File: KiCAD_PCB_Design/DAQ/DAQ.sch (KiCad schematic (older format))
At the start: 92 parts

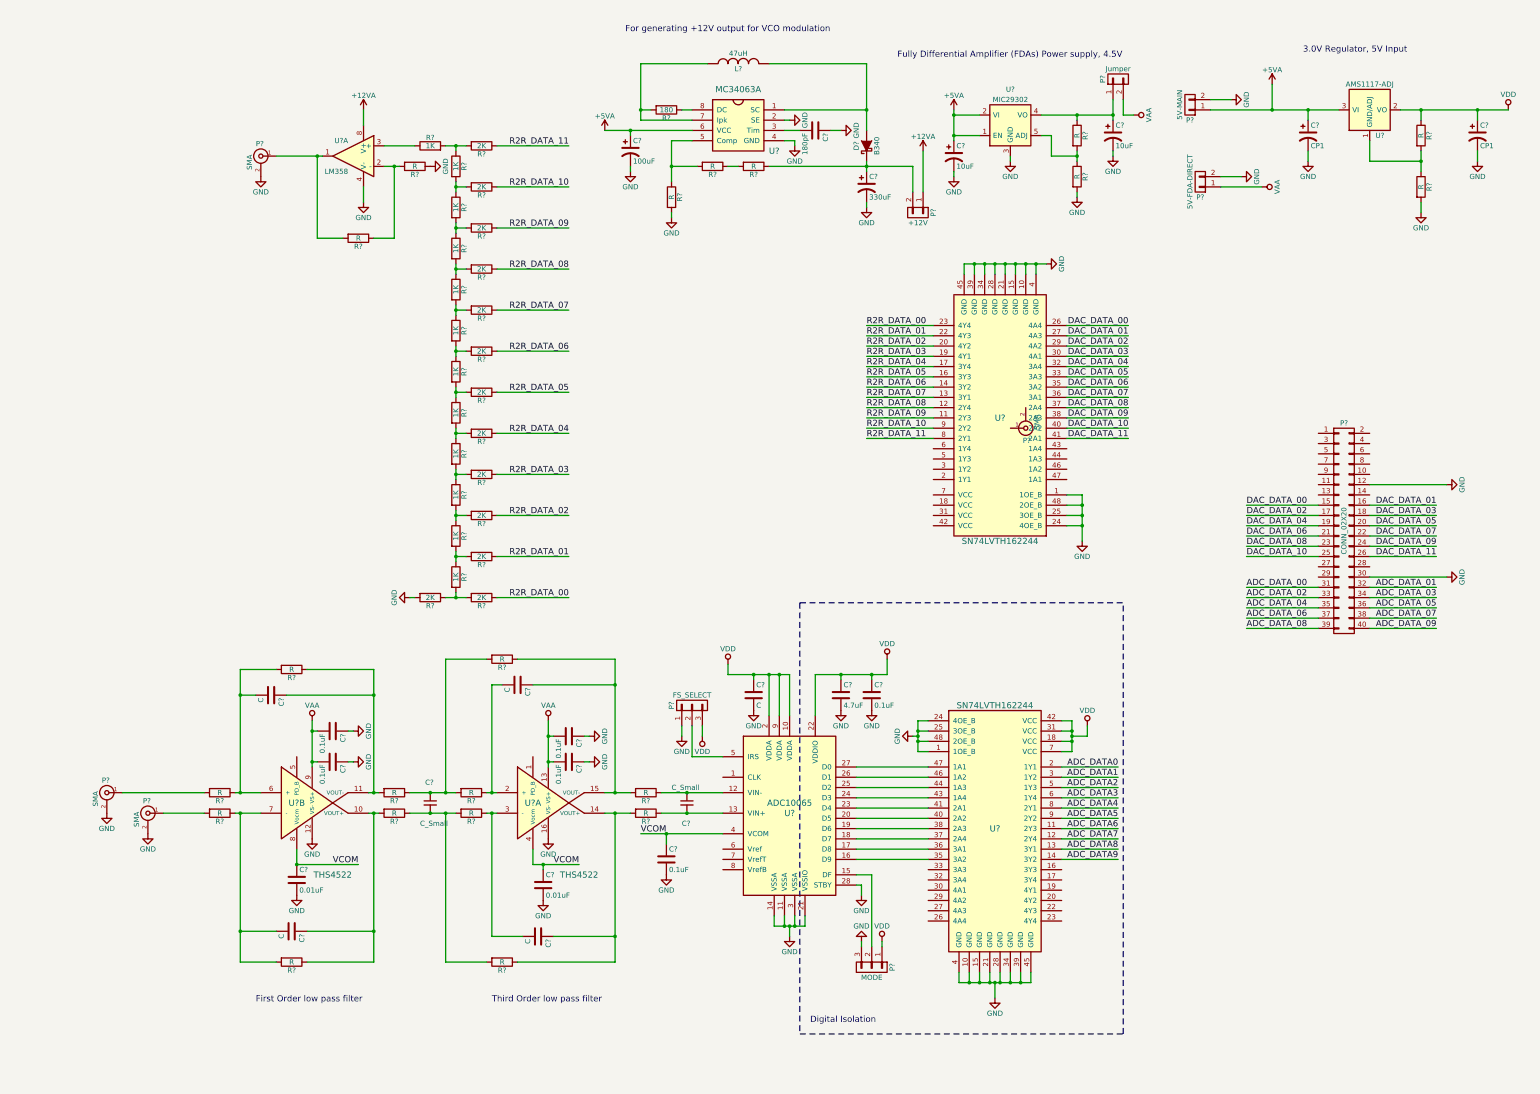
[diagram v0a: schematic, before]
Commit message: Schematic of DAQ.sch is almost complete, Making footprints of SMA, learning about patch array antennas
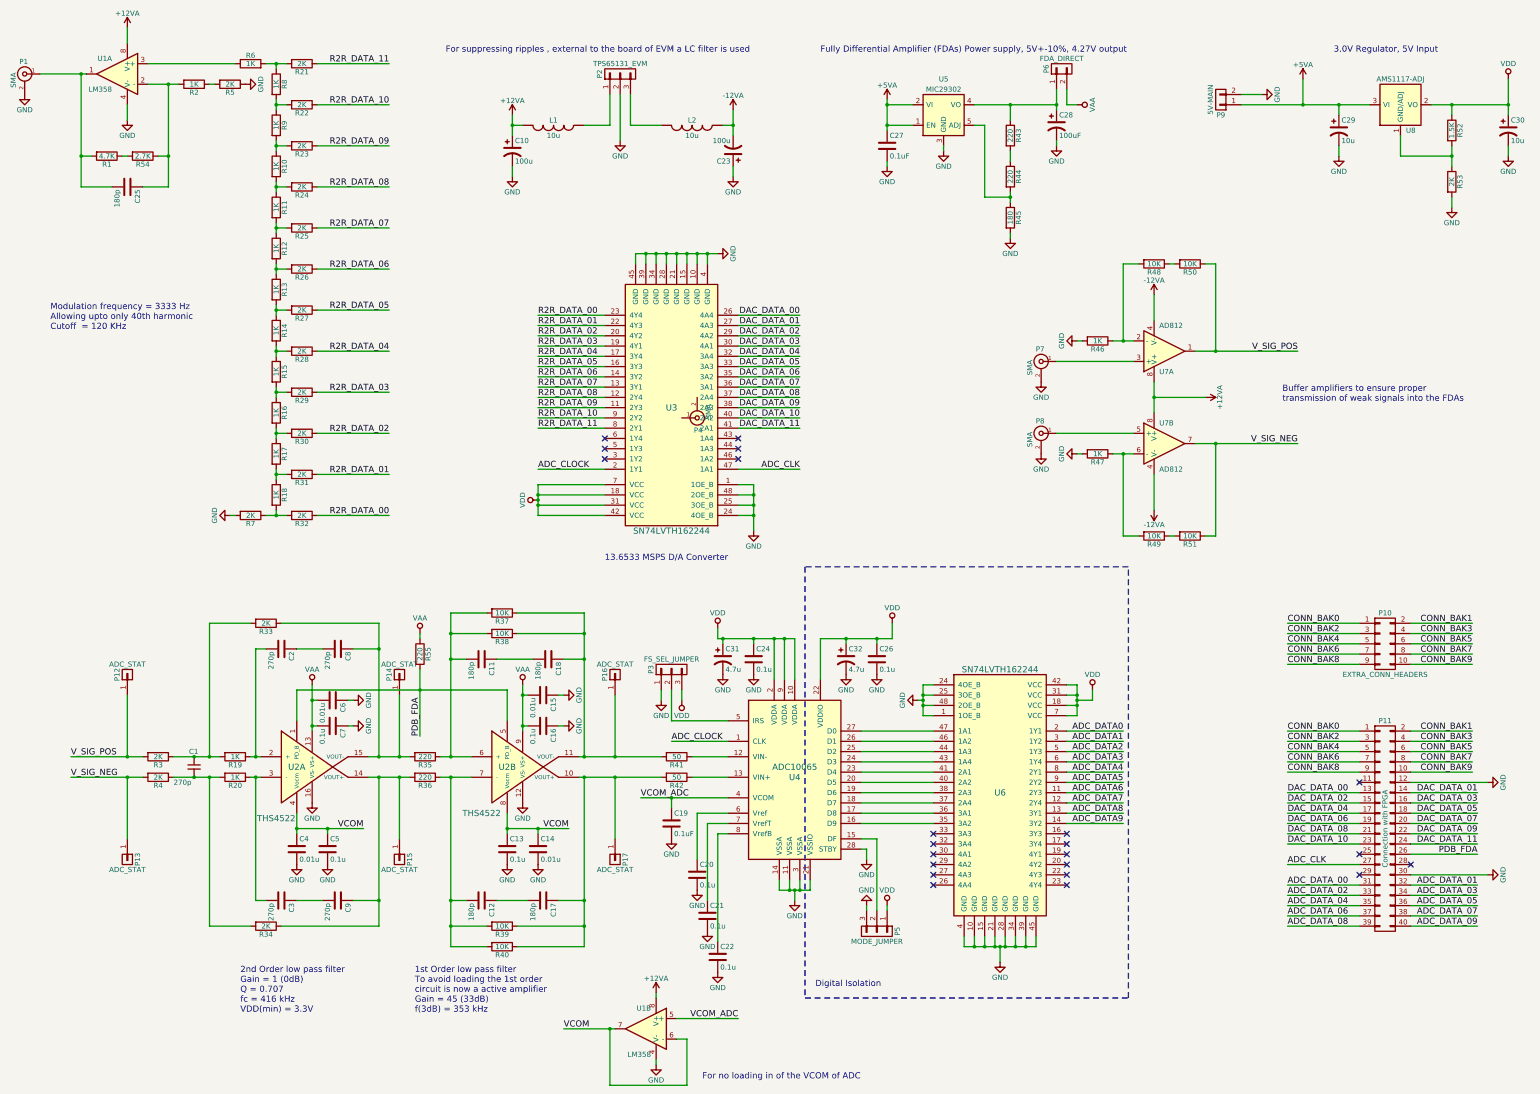
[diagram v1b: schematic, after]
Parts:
- removed C?: 4.7uF, symbol C
- removed C? (x2): C_Small, symbol C_Small
- removed C?: 0.01uF, symbol C
- removed C? (x3): C, symbol C
- removed C?: 10uF, symbol CP1
- removed C?: 100uF, symbol CP1
- removed C?: 330uF, symbol CP1
- removed C?: 180pF, symbol C
- removed D?: B340, symbol D_Schottky
- removed L?: 47uH, symbol INDUCTOR
- removed P?: +12V, symbol CONN_01X02
- removed P?: 5V-FDA-DIRECT, symbol CONN_01X02
- removed R? (x5): R, symbol R
- removed R?: 180, symbol R
- removed U? (x2): THS4522, symbol THS4522
- removed U?: MC34063A, symbol MC34063A
- added C1: 270p, symbol C_Small
- added C10, C23: 100u, symbol CP1
- added C11, C12, C17, C18, C25: 180p, symbol C
- added C13, C20, C21, C22, C5: 0.1u, symbol C
- added C14: 0.01u, symbol C
- added C27: 0.1uF, symbol C
- added C3, C8, C9: 270p, symbol C
- added C31, C32: 4.7u, symbol CP1
- added L1, L2: 10u, symbol INDUCTOR
- added P10: EXTRA_CONN_HEADERS, symbol CONN_02X05
- added P12, P13, P14, P15, P16, P17: ADC_STAT, symbol CONN_01X01
- added P2: TPS65131_EVM, symbol CONN_01X03
- added R2, R46, R47: 1K, symbol R
- added R37, R40, R48, R49, R50, R51: 10K, symbol R
- added R41, R42: 50, symbol R
- added R43, R55: 220, symbol R
- added R54: 2.7K, symbol R
- added unit 2 of U1
- added U2: THS4522, symbol THS4522
- added U7: AD812, symbol LM358
- C15, C6: renamed from C?; value 0.1uF -> 0.01u
- C16, C26, C7: renamed from C?; value 0.1uF -> 0.1u
- C2: renamed from C?; value C -> 270p
- C24: renamed from C?; value C -> 0.1u
- C28: renamed from C?; value 10uF -> 100uF; footprint (none) -> Capacitors_SMD:c_elec_6.3x5.3
- C29, C30: renamed from C?; value CP1 -> 10u
- C4: renamed from C?; value 0.01uF -> 0.01u
- P11: renamed from P?; value CONN_02X20 -> Connection with FPGA
- P3: renamed from P?; value FS_SELECT -> FS_SEL_JUMPER
- P5: renamed from P?; value MODE -> MODE_JUMPER
- P6: renamed from P?; value Jumper -> FDA_DIRECT
- R1: renamed from R?; value R -> 4.7K
- R19, R20: renamed from R?; value R -> 1K
- R3, R33, R34, R4, R5, R53: renamed from R?; value R -> 2K
- R35, R36, R44: renamed from R?; value R -> 220
- R38, R39: renamed from R?; value R -> 10K
- R45: renamed from R?; value R -> 180
- R52: renamed from R?; value R -> 1.5K
- gave numbers to parts that had none: 37
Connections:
- net +12VA: now also C10.1, L1.2, U1.8 (V+), U7.8 (V+), U7.8 (V+)
- net +5VA: now also C27.1
- net DAC_DATA_00: now also P11.13 (P13); no longer P11.15 (P15)
- net DAC_DATA_01: now also P11.14 (P14); no longer P11.16 (P16)
- net DAC_DATA_02: now also P11.15 (P15); no longer P11.17 (P17)
- net DAC_DATA_03: now also P11.16 (P16); no longer P11.18 (P18)
- net DAC_DATA_04: now also P11.17 (P17); no longer P11.19 (P19)
- net DAC_DATA_05: now also P11.18 (P18); no longer P11.20 (P20)
- net DAC_DATA_06: now also P11.19 (P19); no longer P11.21 (P21)
- net DAC_DATA_07: now also P11.20 (P20); no longer P11.22 (P22)
- net DAC_DATA_08: now also P11.21 (P21); no longer P11.23 (P23)
- net DAC_DATA_09: now also P11.22 (P22); no longer P11.24 (P24)
- net DAC_DATA_10: now also P11.23 (P23); no longer P11.25 (P25)
- net DAC_DATA_11: now also P11.24 (P24); no longer P11.26 (P26)
- net GND: now also C10.2, C13.2, C14.2, C20.2, C21.2, C22.2, C23.1, C27.2, C31.2, C32.2, C5.2, P2.2 (P2), R46.2, R47.2, U1.4 (V-), U2.12 (VS-), U2.16 (VS-)
- net VAA: now also R55.1, U2.13 (VS+), U2.9 (VS+)
- net VCOM: now also C13.1, C14.1, C5.1, U1.6 (-), U1.7, U2.4 (Vocm), U2.8 (Vocm); no longer C19.1, U4.4 (VCOM)
- net VDD: now also U3.18 (VCC), U3.31 (VCC), U3.42 (VCC), U3.7 (VCC), C31.1, C32.1
- net CONN_BAK0: now reaches P11.1 (P1)
- net CONN_BAK0: now also P10.1 (P1)
- net CONN_BAK9: now reaches P11.10 (P10)
- net CONN_BAK9: now also P10.10 (P10)
- net CONN_BAK1: now reaches P11.2 (P2)
- net CONN_BAK1: now also P10.2 (P2)
- net ADC_CLK: now reaches P11.27 (P27)
- net ADC_CLK: now also U3.47 (1A1)
- net CONN_BAK2: now reaches P11.3 (P3)
- net CONN_BAK2: now also P10.3 (P3)
- net CONN_BAK3: now reaches P11.4 (P4)
- net CONN_BAK3: now also P10.4 (P4)
- net CONN_BAK4: now reaches P11.5 (P5)
- net CONN_BAK4: now also P10.5 (P5)
- net CONN_BAK5: now reaches P11.6 (P6)
- net CONN_BAK5: now also P10.6 (P6)
- net CONN_BAK6: now reaches P11.7 (P7)
- net CONN_BAK6: now also P10.7 (P7)
- net CONN_BAK7: now reaches P11.8 (P8)
- net CONN_BAK7: now also P10.8 (P8)
- net CONN_BAK8: now reaches P11.9 (P9)
- net CONN_BAK8: now also P10.9 (P9)
- net at P8.1 (In): now also U7.5 (+); no longer R36.2
- net at P7.1 (In): now also U7.3 (+); no longer R35.2
- net ADC_CLOCK: now reaches U4.1 (CLK)
- net ADC_CLOCK: now also U3.2 (1Y1)
- net at U4.12 (VIN-): now also R41.1
- net at U4.13 (VIN+): now also R42.1
- net at U4.6 (Vref): now also C20.1
- net at U4.7 (VrefT): now also C21.1
- net at U4.8 (VrefB): now also C22.1
- net at C2.1: now also C8.2; no longer R33.1
- net at R34.1: now also R36.2, C9.1, P15.1 (P1), U2.14 (VOUT+)
- net at C2.2, R19.1: now also U2.2 (+)
- net at R20.1: now also C3.2, U2.3 (-)
- net at R39.1: now also C17.1, P17.1 (P1), R40.1, R42.2, U2.10 (VOUT+); no longer R4.2
- net at R38.1: now also C18.1, P16.1 (P1), R37.1, R41.2, U2.11 (VOUT-); no longer R3.2
- net at R35.1, R38.2: now also C11.2, R37.2, U2.6 (+)
- net at R36.1, R39.2: now also C12.2, R40.2, U2.7 (-)
- net at R19.2, R3.1, R33.2: now also C1.1
- net at R20.2, R34.2, R4.1: now also C1.2
- net at C28.1, P6.1 (P1), U5.4 (VO): now also R43.1; no longer R44.1
- net at P1.1 (In), R1.2, U1.1: now also C25.2
- new net: C8.1, P14.1 (P1), R33.1, R35.2, U2.15 (VOUT-)
- new net: R43.2, R44.1
- new net: C25.1, R2.2, R54.1, U1.2 (-)
- new net: R2.1, R5.2
- new net: R1.1, R54.2
- new net: C3.1, C9.2
- new net: C11.1, C18.2
- new net: C12.1, C17.2
- new net: R46.1, R48.2, U7.2 (-)
- new net: R47.1, R49.2, U7.6 (-)
- new net: R48.1, R50.2
- new net: R49.1, R51.2
- new net: L1.1, P2.1 (P1)
- new net: L2.2, P2.3 (P3)
- new net -12VA: C23.2, L2.1, U7.4 (V-), U7.4 (V-)
- new net PDB_FDA: P11.26 (P26), R55.2, U2.1 (PD_B), U2.5 (PD_B)
- new net VCOM_ADC: C19.1, U1.5 (+), U4.4 (VCOM)
- new net V_SIG_NEG: P13.1 (P1), R4.2, R51.1, U7.7
- new net V_SIG_POS: P12.1 (P1), R3.2, R50.1, U7.1
- no-connect marks 0 -> 22
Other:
- note added: "13.6533 MSPS D/A Converter\n"
- note added: "1st Order low pass filter\nTo avoid loading the 1st order \ncircuit is now a active amplifier\nGain = 45 (33dB)\nf(3dB) = 353 kHz"
- note added: "2nd Order low pass filter\nGain = 1 (0dB)\nQ = 0.707\nfc = 416 kHz\nVDD(min) = 3.3V"
- note added: "Buffer amplifiers to ensure proper \ntransmission of weak signals into the FDAs"
- note added: "For no loading in of the VCOM of ADC"
- note added: "For suppressing ripples , external to the board of EVM a LC filter is used"
- note added: "Fully Differential Amplifier (FDAs) Power supply, 5V+-10%, 4.27V output"
- note added: "Modulation frequency = 3333 Hz\nAllowing upto only 40th harmonic\nCutoff = 120 KHz"
- note removed: "First Order low pass filter"
- note removed: "For generating +12V output for VCO modulation"
- note removed: "Fully Differential Amplifier (FDAs) Power supply, 4.5V"
- note removed: "Third Order low pass filter"
- moved on the sheet: C15, C16, C19, C2, C24, C26, C28, C29, C30, C4, C6, C7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

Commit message: Routing of the PCB is complete, Now procedding towards zone fills
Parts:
- removed C27: 0.1uF, symbol C
- removed P4: SMA, symbol SMA
- removed U5: MIC29302, symbol MIC29302
- added C27: 10u, Capacitors_Tantalum_SMD:TantalC_SizeS_EIA-3216, symbol CP1
- added C33, C34: 270p, Capacitors_SMD:C_0805_HandSoldering, symbol C
- added C35, C36: 180p, Capacitors_SMD:C_0805_HandSoldering, symbol C
- added C37, C38: 0.1u, Capacitors_SMD:C_0805_HandSoldering, symbol C
- added D1, D2, D3, D4, D5: LED, LEDs:LED_0805, symbol LED
- added P18, P19: ADC_STAT, Pin_Headers:Pin_Header_Straight_1x01, symbol CONN_01X01
- added P20, P21: VCOM_CHECK, Pin_Headers:Pin_Header_Straight_1x01, symbol CONN_01X01
- added R56, R57: 220, Resistors_SMD:R_0805_HandSoldering, symbol R
- added U5: LD1117S33TR, TO_SOT_Packages_SMD:SOT-223, symbol LD1117S33TR
- C1, C11, C12, C13, C14, C15, C16, C17, C18, C19, C2, C20, C21, C22, C24, C25, C26, C3, C4, C5, C6, C7, C8, C9: footprint (none) -> Capacitors_SMD:C_0805_HandSoldering
- C10, C23: value 100u -> 10u; footprint (none) -> Capacitors_SMD:c_elec_3x5.3
- C28: value 100uF -> 10u; footprint Capacitors_SMD:c_elec_6.3x5.3 -> Capacitors_Tantalum_SMD:TantalC_SizeS_EIA-3216
- C29, C30: footprint (none) -> Capacitors_SMD:c_elec_3x5.3
- C31, C32: footprint (none) -> Capacitors_Tantalum_SMD:TantalC_SizeS_EIA-3216
- L1, L2: footprint (none) -> Custom_Footprints:Bourns_Semi_Shielded_Power_Inductor_SRN5040
- P1, P7, P8: footprint (none) -> DAQ:SMA
- P10: footprint (none) -> Pin_Headers:Pin_Header_Straight_2x05
- P11: footprint (none) -> Pin_Headers:Pin_Header_Straight_2x20
- P12, P13, P14, P15, P16, P17: footprint (none) -> Pin_Headers:Pin_Header_Straight_1x01
- P2, P3, P5: footprint (none) -> Pin_Headers:Pin_Header_Straight_1x03
- P6, P9: footprint (none) -> Pin_Headers:Pin_Header_Straight_1x02
- R1, R10, R11, R12, R13, R14, R15, R16, R17, R18, R19, R2, R20, R21, R22, R23, R24, R25, R26, R27, R28, R29, R3, R30, R31, R32, R33, R34, R35, R36, R4, R41, R42, R43, R44, R5, R52, R53, R54, R55, R6, R7, R8, R9: footprint (none) -> Resistors_SMD:R_0805_HandSoldering
- R37, R38, R39, R40, R49, R50, R51: value 10K -> 2.7K; footprint (none) -> Resistors_SMD:R_0805_HandSoldering
- R45: value 180 -> 220; footprint (none) -> Resistors_SMD:R_0805_HandSoldering
- R46, R47: value 1K -> 220; footprint (none) -> Resistors_SMD:R_0805_HandSoldering
- R48: value 10K -> 2.7k; footprint (none) -> Resistors_SMD:R_0805_HandSoldering
- U1, U7: footprint (none) -> Housings_SOIC:SOIC-8_3.9x4.9mm_Pitch1.27mm
- U2: footprint (none) -> Housings_SSOP:TSSOP-16_4.4x5mm_Pitch0.65mm
- U3, U6: footprint (none) -> Housings_SSOP:TSSOP-48_6.1x12.5mm_Pitch0.5mm
- U4: footprint (none) -> Housings_SSOP:TSSOP-28_4.4x9.7mm_Pitch0.65mm
- U8: footprint (none) -> TO_SOT_Packages_SMD:SOT-223
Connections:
- net ADC_DATA0 is gone; now on net ADC_DATA_00: U6.2 (1Y1)
- net ADC_DATA1 is gone; now on net ADC_DATA_01: U6.3 (1Y2)
- net ADC_DATA2 is gone; now on net ADC_DATA_02: U6.5 (1Y3)
- net ADC_DATA3 is gone; now on net ADC_DATA_03: U6.6 (1Y4)
- net ADC_DATA4 is gone; now on net ADC_DATA_04: U6.8 (2Y1)
- net ADC_DATA5 is gone; now on net ADC_DATA_05: U6.9 (2Y2)
- net ADC_DATA6 is gone; now on net ADC_DATA_06: U6.11 (2Y3)
- net ADC_DATA7 is gone; now on net ADC_DATA_07: U6.12 (2Y4)
- net ADC_DATA8 is gone; now on net ADC_DATA_08: U6.13 (3Y1)
- net ADC_DATA9 is gone; now on net ADC_DATA_09: U6.14 (3Y2)
- net +12VA: now also C37.1, D4.2 (A)
- net +5VA: now also C27.1, D2.2 (A), U5.3 (VI)
- net -12VA: now also C38.2, D5.1 (K)
- net GND: now also R43.2, R44.2, C27.2, C37.2, C38.1, R56.2, R57.2, U5.1 (GND)
- net VCOM: now also P20.1 (P1)
- net VCOM_ADC: now also P21.1 (P1)
- net VDD: now also D3.2 (A); no longer U6.18 (VCC), U6.31 (VCC), U6.42 (VCC), U6.7 (VCC)
- net V_SIG_NEG: now also C36.1
- net V_SIG_POS: now also C35.1
- net at U6.35 (3A2): now also U4.27 (D0); no longer U4.16 (D9)
- net at U6.36 (3A1): now also U4.26 (D1); no longer U4.17 (D8)
- net at U6.37 (2A4): now also U4.25 (D2); no longer U4.18 (D7)
- net at U6.38 (2A3): now also U4.24 (D3); no longer U4.19 (D6)
- net at U6.40 (2A2): now also U4.23 (D4); no longer U4.20 (D5)
- net at U6.41 (2A1): now also U4.20 (D5); no longer U4.23 (D4)
- net at U6.43 (1A4): now also U4.19 (D6); no longer U4.24 (D3)
- net at U6.44 (1A3): now also U4.18 (D7); no longer U4.25 (D2)
- net at U6.46 (1A2): now also U4.17 (D8); no longer U4.26 (D1)
- net at U6.47 (1A1): now also U4.16 (D9); no longer U4.27 (D0)
- net at P8.1 (In), U7.5 (+): now also P19.1 (P1)
- net at P7.1 (In), U7.3 (+): now also P18.1 (P1)
- net +3V3: now reaches C28.1, P6.1 (P1)
- net +3V3: now also U6.18 (VCC), U6.31 (VCC), U6.42 (VCC), U6.7 (VCC), D1.2 (A), U5.2 (VO); no longer R43.1
- net at R45.1: now also D3.1 (K); no longer R44.2
- net at C11.2, R35.1, R37.2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: no longer R38.2
- net at C12.2, R36.1, R40.2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: no longer R39.2
- net at C18.1, P16.1 (P1), R41.2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: now also R39.1; no longer R37.1, R38.1
- net at C17.1, P17.1 (P1), R42.2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: now also R38.1; no longer R39.1, R40.1
- net at R44.1: now also D2.1 (K); no longer R43.2
- net at R46.1, R48.2, U7.2 (-): now also C33.2
- net at R47.1, R49.2, U7.6 (-): now also C34.2
- new net: R37.1, R39.2
- new net: C33.1, C35.2
- new net: C34.1, C36.2
- new net: R38.2, R40.1
- new net: D4.1 (K), R56.1
- new net: D5.2 (A), R57.1
- new net: D1.1 (K), R43.1
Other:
- note added: "Buffer amplifiers to ensure proper \ntransmission of weak signals into the FDAs\nCutoff Freq = 300 KHz"
- note added: "FDAs & Digital Buffers Power supply, 5V+-10%, 3.3V output"
- note removed: "Buffer amplifiers to ensure proper \ntransmission of weak signals into the FDAs"
- note removed: "Fully Differential Amplifier (FDAs) Power supply, 5V+-10%, 4.27V output"
- moved on the sheet: C25, P1, P6, P7, P8, R1, R10, R11, R12, R13, R14, R15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

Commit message: All components made except antenna, Now verifying ..
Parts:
- added P4: VCO_SUPPLY, Pin_Headers:Pin_Header_Straight_1x02, symbol CONN_01X02
- U1: value LM358 -> AD812
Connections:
- net GND: now also P4.2 (P2)
- net VDD: now also P4.1 (P1)
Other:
- moved on the sheet: C27, C28, C29, C30, P6, P9, R52, R53, U5, U8
